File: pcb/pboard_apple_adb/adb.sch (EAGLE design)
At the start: 24 parts, among them IC3 STM32F042F4, SW1 324_SW, SW2 324_SW, SW4 324_SW

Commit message: updated ADB board
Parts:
- removed JP2: (no value), pinhead:PINHD-1X6
- added JP5: (no value), pinhead:PINHD-1X5
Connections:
- removed net N$9: IC3.PA3, JP2.1, LED1.A
- net +3V3: now also JP5.4; no longer JP2.5
- net GND: now also JP5.5; no longer JP2.6
- net N$14: now also IC3.PA3
- net N$2: now also LED1.A
- net N$5: now also JP5.3; no longer JP2.4
- net N$6: now also JP5.2; no longer JP2.3
- net N$8: now also JP5.1; no longer JP2.2
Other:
- moved on the sheet: LED1, R2
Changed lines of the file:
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@@
 <part name="+3V5" library="supply1" library_urn="urn:adsk.eagle:library:371" deviceset="+3V3" device=""/>
 <part name="GND5" library="supply1" library_urn="urn:adsk.eagle:library:371" deviceset="GND" device=""/>
-<part name="JP2" library="pinhead" library_urn="urn:adsk.eagle:library:325" deviceset="PINHD-1X6" device="" package3d_urn="urn:adsk.eagle:package:22472/2"/>
 <part name="+3V6" library="supply1" library_urn="urn:adsk.eagle:library:371" deviceset="+3V3" device=""/>
 <part name="GND7" library="supply1" library_urn="urn:adsk.eagle:library:371" deviceset="GND" device=""/>
@@
 <part name="GND17" library="supply1" library_urn="urn:adsk.eagle:library:371" deviceset="GND" device=""/>
 <part name="+3V13" library="supply1" library_urn="urn:adsk.eagle:library:371" deviceset="+3V3" device=""/>
+<part name="JP5" library="pinhead" library_urn="urn:adsk.eagle:library:325" deviceset="PINHD-1X5" device="" package3d_urn="urn:adsk.eagle:package:22469/2"/>
 </parts>
 <sheets>
@@
 <attribute name="VALUE" x="121.92" y="-127" size="1.778" layer="96"/>
 </instance>
-<instance part="JP2" gate="A" x="88.9" y="-149.86" smashed="yes">
-<attribute name="NAME" x="82.55" y="-139.065" size="1.778" layer="95"/>
-<attribute name="VALUE" x="82.55" y="-160.02" size="1.778" layer="96"/>
-</instance>
 <instance part="+3V6" gate="G$1" x="101.6" y="-149.86" smashed="yes">
 <attribute name="VALUE" x="99.06" y="-154.94" size="1.778" layer="96" rot="R90"/>
@@
 <attribute name="VALUE" x="88.9" y="25.4" size="1.778" layer="96" rot="MR0"/>
 </instance>
-<instance part="LED1" gate="G$1" x="109.22" y="-142.24" smashed="yes" rot="R90">
-<attribute name="NAME" x="113.792" y="-138.684" size="1.778" layer="95" rot="R180"/>
-<attribute name="VALUE" x="113.792" y="-136.525" size="1.778" layer="96" rot="R180"/>
-</instance>
-<instance part="R2" gate="G$1" x="119.38" y="-142.24" smashed="yes" rot="R180">
-<attribute name="NAME" x="123.19" y="-143.7386" size="1.778" layer="95" rot="R180"/>
-<attribute name="VALUE" x="123.19" y="-138.938" size="1.778" layer="96" rot="R180"/>
-</instance>
-<instance part="GND12" gate="1" x="129.54" y="-144.78" smashed="yes">
-<attribute name="VALUE" x="127" y="-147.32" size="1.778" layer="96"/>
+<instance part="LED1" gate="G$1" x="162.56" y="-160.02" smashed="yes" rot="R90">
+<attribute name="NAME" x="167.132" y="-156.464" size="1.778" layer="95" rot="R180"/>
+<attribute name="VALUE" x="167.132" y="-154.305" size="1.778" layer="96" rot="R180"/>
+</instance>
+<instance part="R2" gate="G$1" x="172.72" y="-160.02" smashed="yes" rot="R180">
+<attribute name="NAME" x="176.53" y="-161.5186" size="1.778" layer="95" rot="R180"/>
+<attribute name="VALUE" x="176.53" y="-156.718" size="1.778" layer="96" rot="R180"/>
+</instance>
+<instance part="GND12" gate="1" x="182.88" y="-162.56" smashed="yes">
+<attribute name="VALUE" x="180.34" y="-165.1" size="1.778" layer="96"/>
 </instance>
 <instance part="SW2" gate="G$1" x="187.96" y="33.02" smashed="yes" rot="MR270"/>
@@
 <instance part="+3V13" gate="G$1" x="-12.7" y="-55.88" smashed="yes">
 <attribute name="VALUE" x="-15.24" y="-60.96" size="1.778" layer="96" rot="R90"/>
+</instance>
+<instance part="JP5" gate="A" x="88.9" y="-149.86" smashed="yes">
+<attribute name="NAME" x="82.55" y="-141.605" size="1.778" layer="95"/>
+<attribute name="VALUE" x="82.55" y="-160.02" size="1.778" layer="96"/>
 </instance>
 </instances>
@@
 </segment>
 <segment>
-<pinref part="JP2" gate="A" pin="5"/>
 <pinref part="+3V6" gate="G$1" pin="+3V3"/>
 <wire x1="86.36" y1="-152.4" x2="101.6" y2="-152.4" width="0.1524" layer="91"/>
+<pinref part="JP5" gate="A" pin="4"/>
 </segment>
 <segment>
@@
 </segment>
 <segment>
-<pinref part="JP2" gate="A" pin="6"/>
 <pinref part="GND7" gate="1" pin="GND"/>
 <wire x1="86.36" y1="-154.94" x2="78.74" y2="-154.94" width="0.1524" layer="91"/>
+<pinref part="JP5" gate="A" pin="5"/>
 </segment>
 <segment>
@@
 <pinref part="R2" gate="G$1" pin="1"/>
 <pinref part="GND12" gate="1" pin="GND"/>
-<wire x1="129.54" y1="-142.24" x2="124.46" y2="-142.24" width="0.1524" layer="91"/>
+<wire x1="182.88" y1="-160.02" x2="177.8" y2="-160.02" width="0.1524" layer="91"/>
 </segment>
 <segment>
@@
 <wire x1="104.14" y1="-55.88" x2="144.78" y2="-55.88" width="0.1524" layer="91"/>
 <wire x1="144.78" y1="-55.88" x2="144.78" y2="-119.38" width="0.1524" layer="91"/>
+<pinref part="LED1" gate="G$1" pin="A"/>
+<wire x1="160.02" y1="-149.86" x2="160.02" y2="-160.02" width="0.1524" layer="91"/>
+<junction x="160.02" y="-149.86"/>
 </segment>
 </net>
@@
 <wire x1="81.28" y1="-93.98" x2="93.98" y2="-93.98" width="0.1524" layer="91"/>
 <wire x1="93.98" y1="-93.98" x2="93.98" y2="-149.86" width="0.1524" layer="91"/>
-<pinref part="JP2" gate="A" pin="4"/>
 <wire x1="93.98" y1="-149.86" x2="86.36" y2="-149.86" width="0.1524" layer="91"/>
+<pinref part="JP5" gate="A" pin="3"/>
 </segment>
 </net>
@@
 <wire x1="81.28" y1="-114.3" x2="78.74" y2="-114.3" width="0.1524" layer="91"/>
 <wire x1="78.74" y1="-114.3" x2="78.74" y2="-147.32" width="0.1524" layer="91"/>
-<pinref part="JP2" gate="A" pin="3"/>
 <wire x1="78.74" y1="-147.32" x2="86.36" y2="-147.32" width="0.1524" layer="91"/>
+<pinref part="JP5" gate="A" pin="2"/>
 </segment>
 </net>
@@
 <wire x1="81.28" y1="-116.84" x2="76.2" y2="-116.84" width="0.1524" layer="91"/>
 <wire x1="76.2" y1="-116.84" x2="76.2" y2="-144.78" width="0.1524" layer="91"/>
-<pinref part="JP2" gate="A" pin="2"/>
 <wire x1="76.2" y1="-144.78" x2="86.36" y2="-144.78" width="0.1524" layer="91"/>
-</segment>
-</net>
-<net name="N$9" class="0">
-<segment>
-<pinref part="JP2" gate="A" pin="1"/>
-<wire x1="96.52" y1="-142.24" x2="86.36" y2="-142.24" width="0.1524" layer="91"/>
-<pinref part="IC3" gate="G$1" pin="PA3"/>
-<wire x1="81.28" y1="-96.52" x2="96.52" y2="-96.52" width="0.1524" layer="91"/>
-<wire x1="96.52" y1="-96.52" x2="96.52" y2="-142.24" width="0.1524" layer="91"/>
-<pinref part="LED1" gate="G$1" pin="A"/>
-<wire x1="96.52" y1="-142.24" x2="106.68" y2="-142.24" width="0.1524" layer="91"/>
-<junction x="96.52" y="-142.24"/>
+<pinref part="JP5" gate="A" pin="1"/>
 </segment>
 </net>
@@
 <wire x1="78.74" y1="17.78" x2="96.52" y2="17.78" width="0.1524" layer="91"/>
 <junction x="96.52" y="17.78"/>
-</segment>
-</net>
+<wire x1="78.74" y1="17.78" x2="38.1" y2="17.78" width="0.1524" layer="91"/>
+<wire x1="38.1" y1="17.78" x2="38.1" y2="-96.52" width="0.1524" layer="91"/>
+<junction x="78.74" y="17.78"/>
+<pinref part="IC3" gate="G$1" pin="PA3"/>
+<wire x1="38.1" y1="-96.52" x2="81.28" y2="-96.52" width="0.1524" layer="91"/>
+</segment>
+</net>

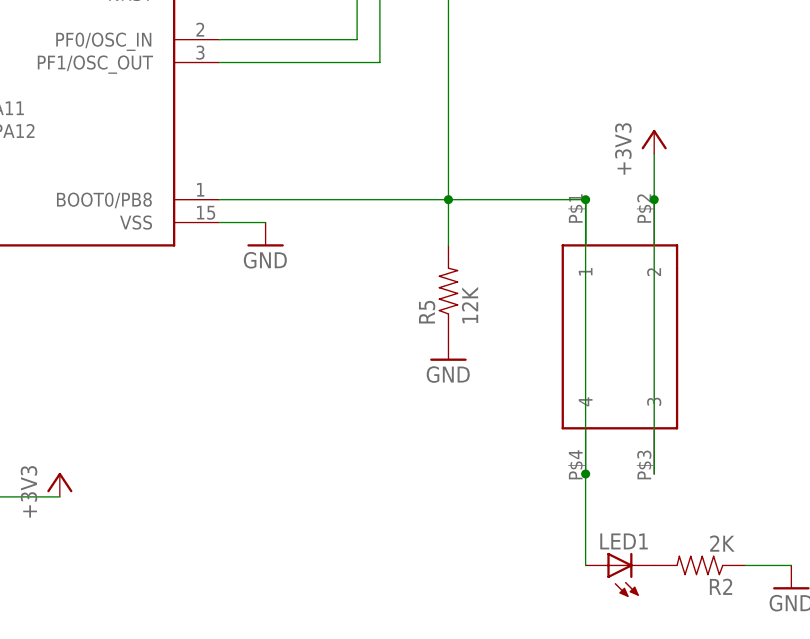
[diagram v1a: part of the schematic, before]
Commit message: porting ADB code to new board
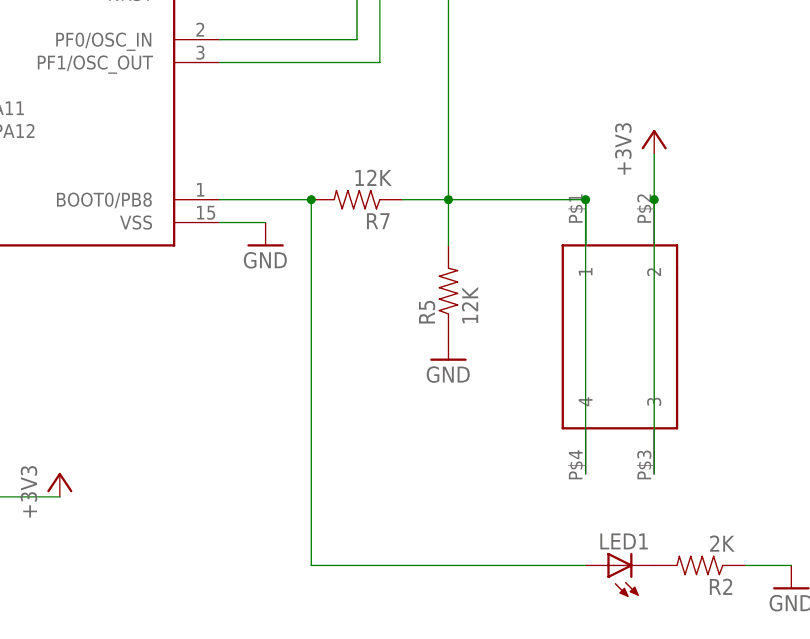
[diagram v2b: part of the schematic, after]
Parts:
- added R7: 12K, SparkFun-Passives:RESISTOR0805-RES
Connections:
- new net N$9: IC3.BOOT0/PB8, LED1.A, R7.2
- net N$2: now also R7.1; no longer IC3.BOOT0/PB8, LED1.A
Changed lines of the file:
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@@
 <part name="+3V13" library="supply1" library_urn="urn:adsk.eagle:library:371" deviceset="+3V3" device=""/>
 <part name="JP5" library="pinhead" library_urn="urn:adsk.eagle:library:325" deviceset="PINHD-1X5" device="" package3d_urn="urn:adsk.eagle:package:22469/2"/>
+<part name="R7" library="SparkFun-Passives" deviceset="RESISTOR" device="0805-RES" value="12K"/>
 </parts>
 <sheets>
@@
 <attribute name="NAME" x="82.55" y="-141.605" size="1.778" layer="95"/>
 <attribute name="VALUE" x="82.55" y="-160.02" size="1.778" layer="96"/>
+</instance>
+<instance part="R7" gate="G$1" x="134.62" y="-119.38" smashed="yes" rot="R180">
+<attribute name="NAME" x="138.43" y="-120.8786" size="1.778" layer="95" rot="R180"/>
+<attribute name="VALUE" x="138.43" y="-116.078" size="1.778" layer="96" rot="R180"/>
 </instance>
 </instances>
@@
 <pinref part="R5" gate="G$1" pin="2"/>
 <wire x1="144.78" y1="-119.38" x2="144.78" y2="-124.46" width="0.1524" layer="91"/>
-<pinref part="IC3" gate="G$1" pin="BOOT0/PB8"/>
-<wire x1="119.38" y1="-119.38" x2="144.78" y2="-119.38" width="0.1524" layer="91"/>
 <pinref part="SW1" gate="G$1" pin="1"/>
+<wire x1="139.7" y1="-119.38" x2="144.78" y2="-119.38" width="0.1524" layer="91"/>
 <wire x1="160.02" y1="-124.46" x2="160.02" y2="-119.38" width="0.1524" layer="91"/>
 <pinref part="SW1" gate="G$1" pin="4"/>
@@
 <wire x1="104.14" y1="-55.88" x2="144.78" y2="-55.88" width="0.1524" layer="91"/>
 <wire x1="144.78" y1="-55.88" x2="144.78" y2="-119.38" width="0.1524" layer="91"/>
-<pinref part="LED1" gate="G$1" pin="A"/>
-<wire x1="160.02" y1="-149.86" x2="160.02" y2="-160.02" width="0.1524" layer="91"/>
-<junction x="160.02" y="-149.86"/>
+<pinref part="R7" gate="G$1" pin="1"/>
 </segment>
 </net>
@@
 </segment>
 </net>
+<net name="N$9" class="0">
+<segment>
+<pinref part="R7" gate="G$1" pin="2"/>
+<pinref part="IC3" gate="G$1" pin="BOOT0/PB8"/>
+<wire x1="119.38" y1="-119.38" x2="129.54" y2="-119.38" width="0.1524" layer="91"/>
+<pinref part="LED1" gate="G$1" pin="A"/>
+<wire x1="160.02" y1="-160.02" x2="129.54" y2="-160.02" width="0.1524" layer="91"/>
+<wire x1="129.54" y1="-160.02" x2="129.54" y2="-119.38" width="0.1524" layer="91"/>
+<junction x="129.54" y="-119.38"/>
+</segment>
+</net>

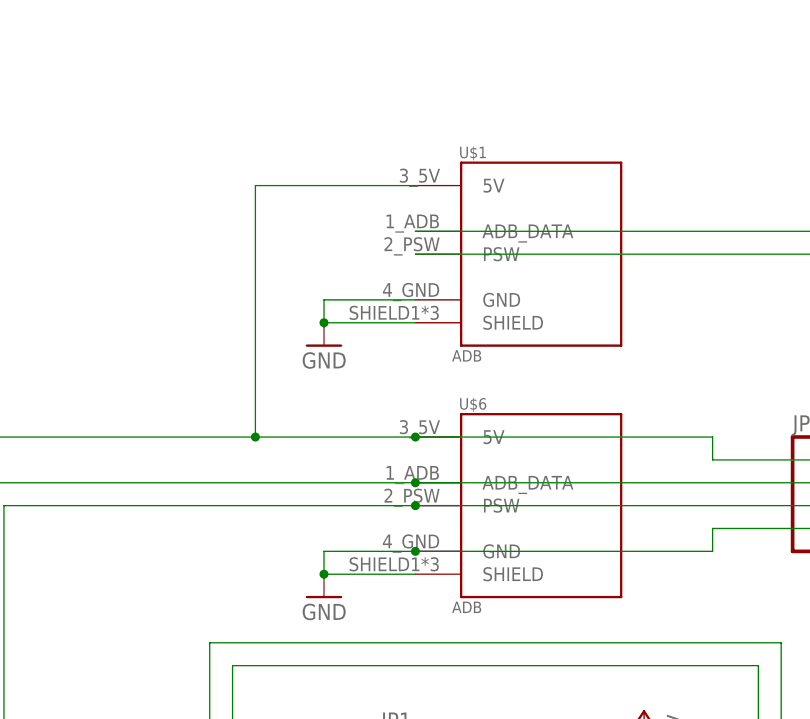
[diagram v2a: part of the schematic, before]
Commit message: fixed flipped ADB connector footprint
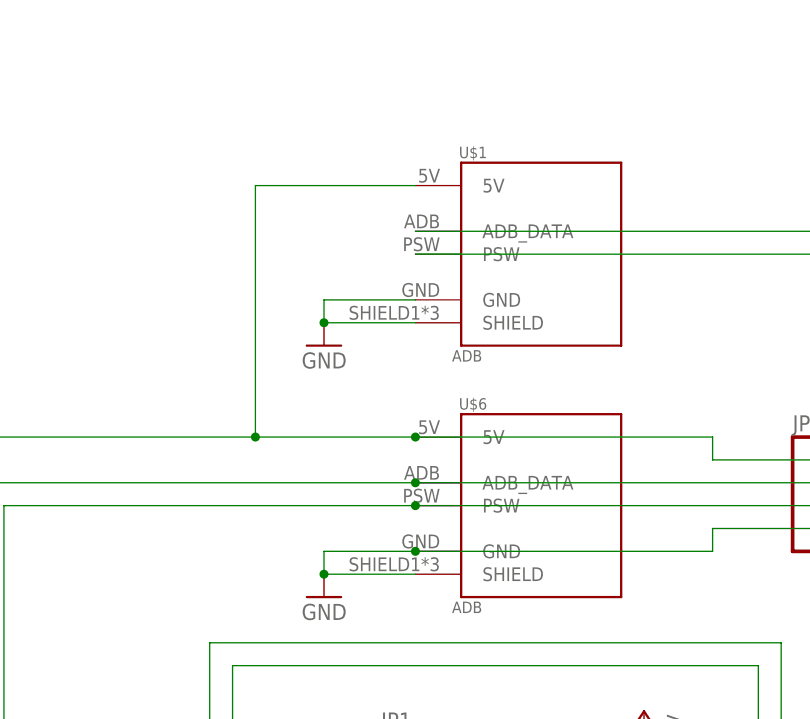
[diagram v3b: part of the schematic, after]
